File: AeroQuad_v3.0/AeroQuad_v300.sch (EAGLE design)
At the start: 68 parts, among them U1 MPU-6050-1

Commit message: Eagle files including CAM file for latest beta run of AeroQuad32 boards.
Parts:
- removed ACCEL: BMA180, SparkFun:M08LOCK
- removed GYRO: ITG3200, SparkFun:M07LOCK
- removed LED: ULN2003A, CaranchoEngineering:ULN2003A
- removed LED_GND, LED_PWR: (no value), SparkFun:M07LOCK
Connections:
- removed net N$10: LED.P$10, LED_GND.7
- removed net N$11: LED.P$11, LED_GND.6
- removed net N$12: LED.P$12, LED_GND.5
- removed net N$13: LED.P$13, LED_GND.4
- removed net N$14: LED.P$14, LED_GND.3
- removed net N$17: LED.P$15, LED_GND.2
- removed net P$16: LED.P$16, LED_GND.1
- net 3.3V: no longer ACCEL.1, ACCEL.4, ACCEL.8, GYRO.6, GYRO.7
- net GND: no longer ACCEL.2, ACCEL.6, GYRO.3, GYRO.5, LED.P$8
- net LED1: no longer LED.P$7
- net LED2: no longer LED.P$6
- net LED3: no longer LED.P$5
- net LED4: no longer LED.P$4
- net LED5: no longer LED.P$3
- net LED6: no longer LED.P$2
- net LED7: no longer LED.P$1
- net SCL-L: no longer ACCEL.5, GYRO.1
- net SDA-L: no longer ACCEL.7, GYRO.2
- net VIN: no longer LED_PWR.1, LED_PWR.2, LED_PWR.3, LED_PWR.4, LED_PWR.5, LED_PWR.6, LED_PWR.7

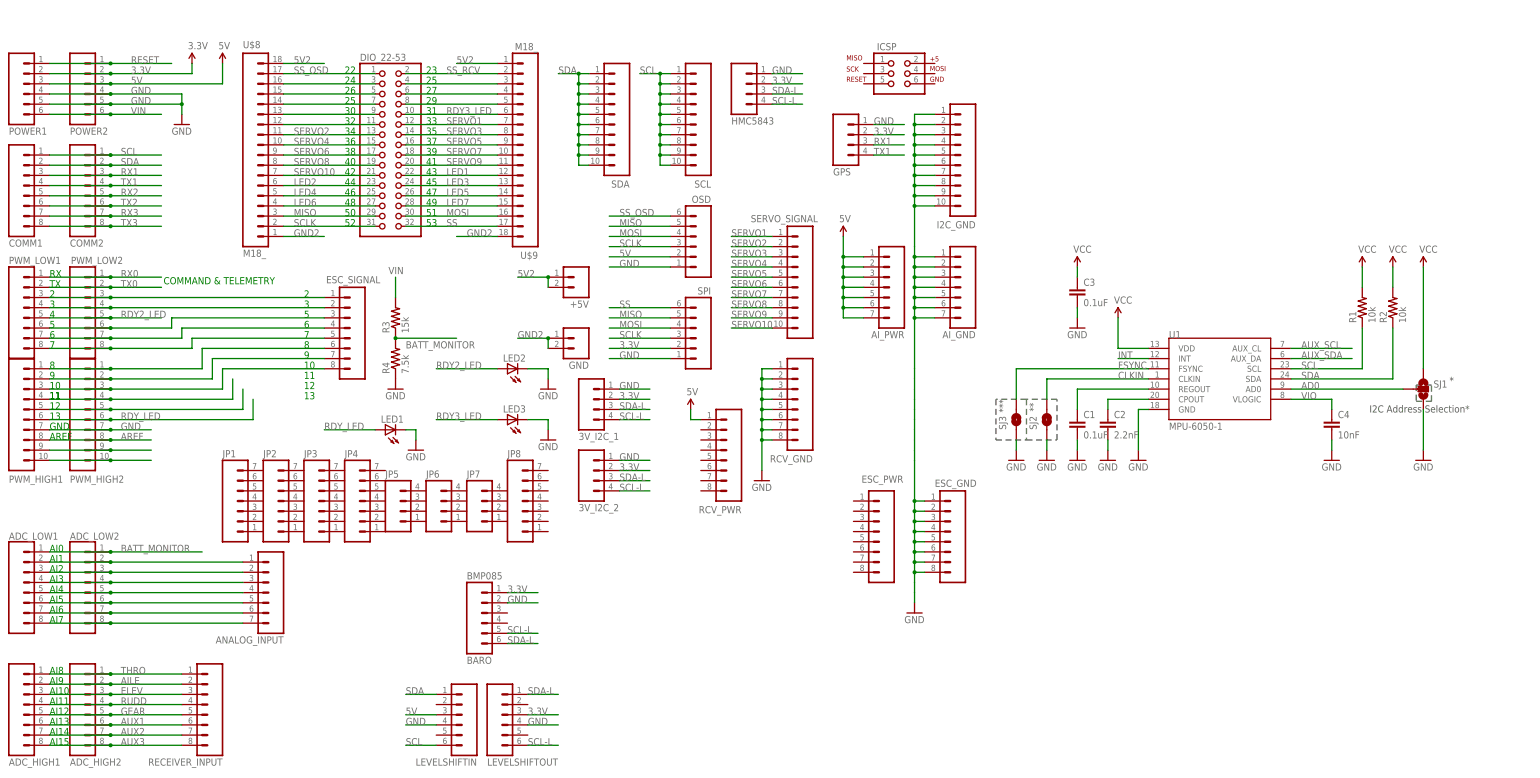
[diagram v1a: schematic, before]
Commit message: reviewed MPU6000 circuit and connections to Due
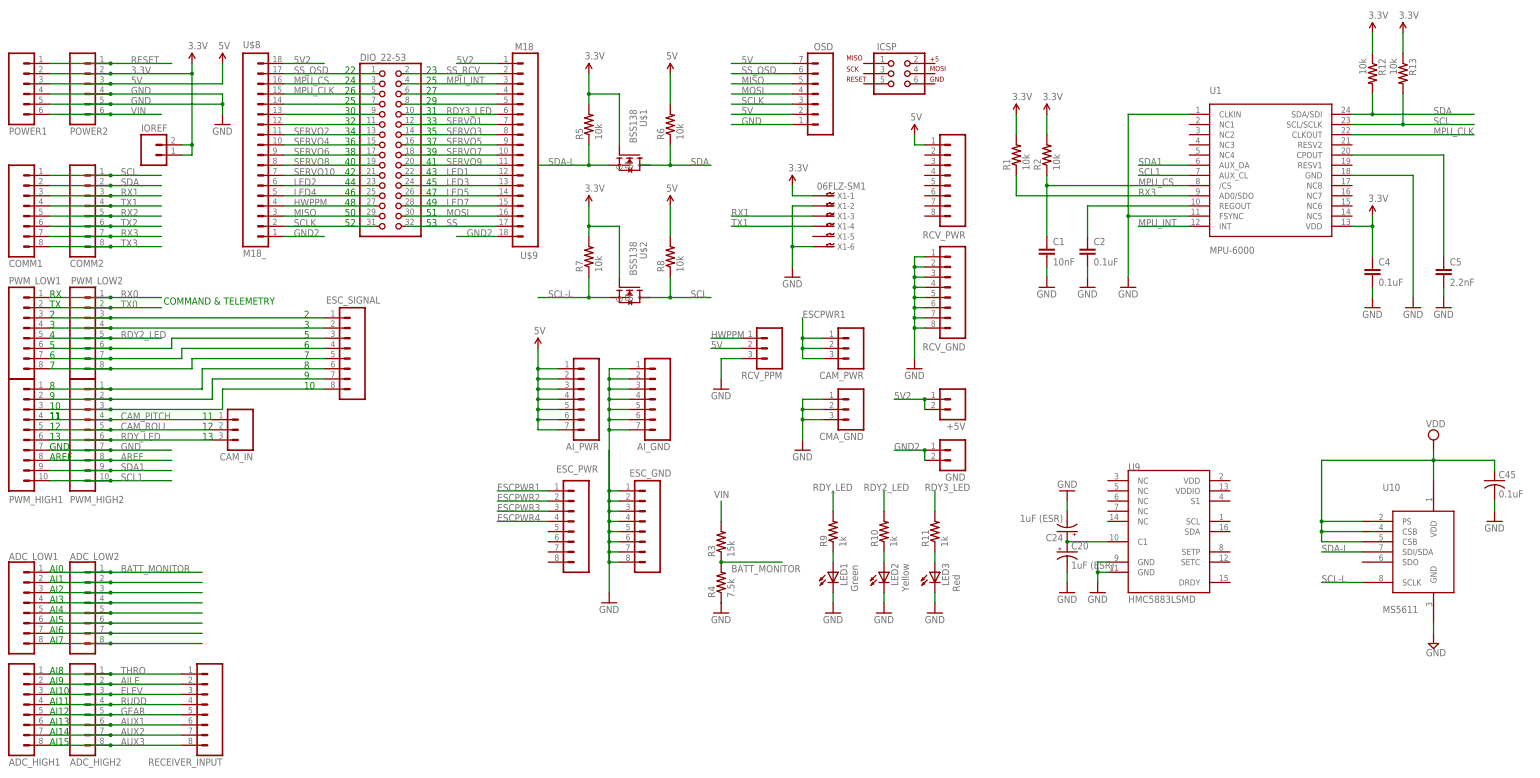
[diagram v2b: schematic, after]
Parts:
- removed 3V_I2C_1, 3V_I2C_2, GPS, HMC5843: (no value), SparkFun:M04LOCK
- removed ANALOG_INPUT, JP1, JP2, JP3, JP4, JP8: (no value), SparkFun:M07
- removed BARO: BMP085, SparkFun:M06LOCK
- removed C3: 0.1uF, SparkFun:CAP0402-CAP
- removed I2C_GND, SCL, SDA, SERVO_SIGNAL: M10LOCK, SparkFun:M10LOCK
- removed JP5, JP6, JP7: (no value), SparkFun:M04PTH
- removed LEVELSHIFTIN, LEVELSHIFTOUT, SPI: (no value), SparkFun:M06LOCK
- removed SJ1: (no value), SparkFun:SOLDERJUMPER_2WAYPASTE2&3
- removed SJ2, SJ3: SOLDERJUMPERTRACE, SparkFun:SOLDERJUMPERTRACE
- added C20, C24: 1uF (ESR), rcl:CPOL-USSMCZ
- added C45: 0.1uF, rcl:C-USC0402
- added C5: 2.2nF, SparkFun:CAP0402-CAP
- added CAM_IN, CAM_PWR, CMA_GND, RCV_PPM: (no value), SparkFun:M03LOCK
- added IOREF: (no value), SparkFun:M02LOCK
- added R10, R11, R9: 1k, SparkFun:RESISTOR0402-RES
- added R12, R13, R5, R6, R7, R8: 10k, SparkFun:RESISTOR0402-RES
- added U$1, U$2: BSS138, ava:BSS138
- added U10: MS5611, DSP-TI:MS5611
- added U9: HMC5883LSMD, SparkFun:HMC5883LSMD
- added X1: 06FLZ-SM1, con-jst:06FLZ-SM1
- C1: value 0.1uF -> 10nF
- C2: value 2.2nF -> 0.1uF
- C4: value 10nF -> 0.1uF
- LED1: value (none) -> Green; device SparkFun:LED5MM -> SparkFun:LED0603
- LED2: value (none) -> Yellow; device SparkFun:LED5MM -> SparkFun:LED0603
- LED3: value (none) -> Red; device SparkFun:LED5MM -> SparkFun:LED0603
- OSD: device SparkFun:M06LOCK -> SparkFun:M07LOCK
- R3, R4: device resistor:R-US_0204/5 -> SparkFun:RESISTOR0402-RES
- U1: value MPU-6050-1 -> MPU-6000; device Testing:MPU-6050-1 -> 3DRobotics_Master_Library:MPU-6000
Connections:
- removed net AD0: SJ1.2, U1.AD0
- removed net AUX_SCL: U1.AUX_CL
- removed net AUX_SDA: U1.AUX_DA
- removed net CLKIN: SJ2.2, U1.CLKIN
- removed net FSYNC: SJ3.2, U1.FSYNC
- removed net INT: U1.INT
- removed net LED6: DIO_22-53.27, U$8.4
- removed net N$15: DIO_22-53.3, U$8.16
- removed net N$20: DIO_22-53.5, U$8.15
- removed net N$22: DIO_22-53.4, U$9.3
- removed net N$28: PWM_HIGH1.4, PWM_HIGH2.4
- removed net N$29: PWM_HIGH1.5, PWM_HIGH2.5
- removed net N$30: PWM_HIGH1.9, PWM_HIGH2.9
- removed net N$31: PWM_HIGH1.10, PWM_HIGH2.10
- removed net N$32: C2.1, U1.CPOUT
- removed net VCC: C3.1, R1.2, R2.2, SJ1.1, U1.VDD
- removed net VIO: C4.1, U1.VLOGIC
- new net 3V3DIG: C45.1, U10.CSB, U10.CSB@2, U10.PS, U10.VDD
- new net CAM_PITCH: CAM_IN.1, PWM_HIGH1.4, PWM_HIGH2.4
- new net CAM_ROLL: CAM_IN.2, PWM_HIGH1.5, PWM_HIGH2.5
- new net ESCPWR1: CAM_PWR.1, CAM_PWR.2, CAM_PWR.3, ESC_PWR.1
- new net ESCPWR2: ESC_PWR.2
- new net ESCPWR3: ESC_PWR.3
- new net ESCPWR4: ESC_PWR.4
- new net HWPPM: DIO_22-53.27, RCV_PPM.1, U$8.4
- new net MPU_CLK: DIO_22-53.5, U$8.15, U1.CLKOUT
- new net MPU_CS: C1.1, DIO_22-53.3, R2.1, U$8.16, U1./CS
- new net MPU_INT: DIO_22-53.4, U$9.3, U1.INT
- new net N$10: LED1.A, R9.1
- new net N$11: LED2.A, R10.1
- new net N$12: LED3.A, R11.1
- new net N$40: C5.1, U1.CPOUT
- new net N$67: C20.+, C24.+, U9.C1
- new net SCL1: PWM_HIGH1.10, PWM_HIGH2.10, U1.AUX_CL
- new net SDA1: PWM_HIGH1.9, PWM_HIGH2.9, U1.AUX_DA
- net 3.3V: now also C4.1, IOREF.1, IOREF.2, R1.2, R12.1, R13.1, R2.2, R5.2, R7.2, U$1.G, U$2.G, U1.VDD, X1-1.1; no longer 3V_I2C_1.2, 3V_I2C_2.2, BARO.1, GPS.2, HMC5843.2, LEVELSHIFTOUT.3, SPI.2
- net 5V: now also OSD.7, R6.2, R8.2, RCV_PPM.2; no longer LEVELSHIFTIN.3
- net GND: now also C20.-, C24.-, C45.2, C5.2, CMA_GND.1, CMA_GND.2, CMA_GND.3, RCV_PPM.3, U1.CLKIN, U1.FSYNC, U10.GND, U9.GND@1, U9.GND@2, X1-2.1, X1-6.1; no longer 3V_I2C_1.1, 3V_I2C_2.1, BARO.2, C3.2, GPS.1, HMC5843.1, I2C_GND.1, I2C_GND.10, I2C_GND.2, I2C_GND.3, I2C_GND.4, I2C_GND.5, I2C_GND.6, I2C_GND.7, I2C_GND.8, I2C_GND.9, LEVELSHIFTIN.4, LEVELSHIFTOUT.4, SJ1.3, SJ2.1, SJ3.1, SPI.1
- net MISO: no longer SPI.5
- net MOSI: no longer SPI.4
- net N$18: no longer ANALOG_INPUT.6
- net N$19: no longer ANALOG_INPUT.7
- net N$33: now also C2.1; no longer C1.1
- net N$4: no longer ANALOG_INPUT.1
- net N$6: no longer ANALOG_INPUT.2
- net N$7: no longer ANALOG_INPUT.3
- net N$8: no longer ANALOG_INPUT.4
- net N$9: no longer ANALOG_INPUT.5
- net RDY2_LED: now also R10.2; no longer LED2.A
- net RDY3_LED: now also R11.2; no longer LED3.A
- net RDY_LED: now also CAM_IN.3, R9.2; no longer LED1.A
- net RX1: now also X1-3.1; no longer GPS.3
- net RX3: now also R1.1, U1.AD0/SDO
- net SCL: now also R13.2, R8.1, U$2.D, U1.SCL/SCLK; no longer LEVELSHIFTIN.6, R1.1, SCL.1, SCL.10, SCL.2, SCL.3, SCL.4, SCL.5, SCL.6, SCL.7, SCL.8, SCL.9, U1.SCL
- net SCL-L: now also R7.1, U$2.S, U10.SCLK; no longer 3V_I2C_1.4, 3V_I2C_2.4, BARO.5, HMC5843.4, LEVELSHIFTOUT.6
- net SCLK: no longer SPI.3
- net SDA: now also R12.2, R6.1, U$1.D, U1.SDA/SDI; no longer LEVELSHIFTIN.1, R2.1, SDA.1, SDA.10, SDA.2, SDA.3, SDA.4, SDA.5, SDA.6, SDA.7, SDA.8, SDA.9, U1.SDA
- net SDA-L: now also R5.1, U$1.S, U10.SDI/SDA; no longer 3V_I2C_1.3, 3V_I2C_2.3, BARO.6, HMC5843.3, LEVELSHIFTOUT.1
- net SERVO1: no longer SERVO_SIGNAL.1
- net SERVO10: no longer SERVO_SIGNAL.10
- net SERVO2: no longer SERVO_SIGNAL.2
- net SERVO3: no longer SERVO_SIGNAL.3
- net SERVO4: no longer SERVO_SIGNAL.4
- net SERVO5: no longer SERVO_SIGNAL.5
- net SERVO6: no longer SERVO_SIGNAL.6
- net SERVO7: no longer SERVO_SIGNAL.7
- net SERVO8: no longer SERVO_SIGNAL.8
- net SERVO9: no longer SERVO_SIGNAL.9
- net SS: no longer SPI.6
- net TX1: now also X1-4.1; no longer GPS.4
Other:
- note removed: "*"
- note removed: "**"
- note removed: "***"
- note removed: "I2C Address Selection*"
- moved on the sheet: +5V, ADC_LOW1, ADC_LOW2, AI_GND, AI_PWR, C1, C2, C4, COMM1, COMM2, ESC_GND, ESC_PWR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

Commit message: updated v2.1.3 shield with fixed 3.3V for GPS and added 5V reset line for OSD
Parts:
- removed C20, C24: 1uF (ESR), rcl:CPOL-USSMCZ
- removed C45: 0.1uF, rcl:C-USC0402
- removed R13: 10k, SparkFun:RESISTOR0402-RES
- added C3, C7: 0.1uF, SparkFun:CAP0402-CAP
- added C6: 0.22uF, SparkFun:CAP0402-CAP
- added C8: 100nF, SparkFun:CAP0402-CAP
- added EXT_MAG, GPS: (no value), SparkFun:M04LOCK
- added GPSBAT: (no value), SparkFun:M02PTH
- added LED4: Green, SparkFun:LED0603
- C4: value 0.1uF -> 2.2nF
- C5: value 2.2nF -> 4.7uF
- R12: value 10k -> 1k
- renumbered CMA_GND to CAM_GND
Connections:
- net N$18 renamed AI6
- net N$19 renamed AI7
- net N$4 renamed AI1
- net N$6 renamed AI2
- net N$7 renamed AI3
- net N$8 renamed AI4
- net N$9 renamed AI5
- removed net 3V3DIG: C45.1, U10.CSB, U10.CSB@2, U10.PS, U10.VDD
- removed net N$67: C20.+, C24.+, U9.C1
- new net GLED: R12.2, X1-6.1
- new net N$13: C5.1, U9.C1
- new net N$14: EXT_MAG.4, U1.AUX_CL
- new net N$15: EXT_MAG.3, U1.AUX_DA
- new net N$17: IOREF.1, IOREF.2
- new net N$20: C6.1, U9.SETP
- new net N$22: C6.2, U9.SETC
- new net N$4: LED4.A, R12.1
- new net N$8: GPSBAT.2, X1-5.1
- net 3.3V: now also C3.1, C7.1, C8.1, EXT_MAG.2, GPS.1, U10.CSB, U10.CSB@2, U10.PS, U10.VDD, U9.S1, U9.VDD, U9.VDDIO, X1-4.1; no longer C4.1, IOREF.1, IOREF.2, R12.1, R13.1, X1-1.1
- net GND: now also C3.2, C7.2, C8.2, EXT_MAG.1, GPS.2, GPSBAT.1, LED4.C, X1-3.1; no longer C20.-, C24.-, C45.2, X1-2.1, X1-6.1
- net N$40: now also C4.1; no longer C5.1
- net RX1: now also GPS.3, X1-2.1; no longer X1-3.1
- net SCL: no longer R13.2, U1.SCL/SCLK
- net SCL-L: now also U1.SCL/SCLK, U9.SCL
- net SCL1: no longer U1.AUX_CL
- net SDA: no longer R12.2, U1.SDA/SDI
- net SDA-L: now also U1.SDA/SDI, U9.SDA
- net SDA1: no longer U1.AUX_DA
- net TX1: now also GPS.4, X1-1.1; no longer X1-4.1
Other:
- note added: "GPS"
- note added: "LED"
- note added: "VBAT"
- note added: "VIN"
- moved on the sheet: AI_GND, AI_PWR, C1, C2, C4, C5, ESC_GND, ESC_PWR, R1, R12, R2, R3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

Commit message: Begin work on Due compatible AQ shield
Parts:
- removed R5, R6, R7, R8: 10k, SparkFun:RESISTOR0402-RES
- removed U$1, U$2: BSS138, ava:BSS138
- added IC3: 74245MTC, adafruit:74245MTC
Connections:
- removed net CAM_PITCH: CAM_IN.1, PWM_HIGH1.4, PWM_HIGH2.4
- removed net CAM_ROLL: CAM_IN.2, PWM_HIGH1.5, PWM_HIGH2.5
- removed net HWPPM: DIO_22-53.27, RCV_PPM.1, U$8.4
- removed net N$16: ESC_SIGNAL.3, PWM_LOW1.6, PWM_LOW2.6
- removed net N$21: ESC_SIGNAL.1, PWM_LOW1.3, PWM_LOW2.3
- removed net N$23: ESC_SIGNAL.4, PWM_LOW1.7, PWM_LOW2.7
- removed net N$24: ESC_SIGNAL.5, PWM_LOW1.8, PWM_LOW2.8
- removed net N$25: ESC_SIGNAL.6, PWM_HIGH1.1, PWM_HIGH2.1
- removed net N$26: ESC_SIGNAL.7, PWM_HIGH1.2, PWM_HIGH2.2
- removed net N$27: ESC_SIGNAL.8, PWM_HIGH1.3, PWM_HIGH2.3
- removed net SCL: COMM1.1, COMM2.1, R8.1, U$2.D
- removed net SDA: COMM1.2, COMM2.2, R6.1, U$1.D
- removed net SERVO2: DIO_22-53.13, U$8.11
- removed net SERVO4: DIO_22-53.15, U$8.10
- removed net SERVO6: DIO_22-53.17, U$8.9
- removed net SERVO8: DIO_22-53.19, U$8.8
- new net PWM10: IC3A.A5, PWM_HIGH1.3, PWM_HIGH2.3
- new net PWM11: IC3A.A6, PWM_HIGH1.4, PWM_HIGH2.4
- new net PWM12: IC3A.A7, PWM_HIGH1.5, PWM_HIGH2.5
- new net PWM13: IC3A.A8, PWM_HIGH1.6, PWM_HIGH2.6
- new net PWM2: IC3A.A1, PWM_LOW1.3, PWM_LOW2.3
- new net PWM3: IC3A.A2, PWM_LOW1.4, PWM_LOW2.4
- new net PWM34: DIO_22-53.13, ESC_SIGNAL.4, U$8.11
- new net PWM36: DIO_22-53.15, ESC_SIGNAL.3, U$8.10
- new net PWM38: DIO_22-53.17, ESC_SIGNAL.2, U$8.9
- new net PWM4: IC3A.A3, PWM_LOW1.5, PWM_LOW2.5
- new net PWM40: DIO_22-53.19, ESC_SIGNAL.1, U$8.8
- new net PWM5: IC3A.A4, PWM_LOW1.6, PWM_LOW2.6
- new net PWM6: ESC_SIGNAL.5, PWM_LOW1.7, PWM_LOW2.7
- new net PWM7: ESC_SIGNAL.6, PWM_LOW1.8, PWM_LOW2.8
- new net PWM8: ESC_SIGNAL.7, PWM_HIGH1.1, PWM_HIGH2.1
- new net PWM9: ESC_SIGNAL.8, PWM_HIGH1.2, PWM_HIGH2.2
- net 3.3V: now also IC3P.VCC; no longer R5.2, R7.2, U$1.G, U$2.G
- net 5V: no longer R6.2, R8.2
- net AILE: now also IC3A.B7; no longer ADC_HIGH1.2, ADC_HIGH2.2
- net AUX1: now also IC3A.B3; no longer ADC_HIGH1.6, ADC_HIGH2.6
- net AUX2: now also IC3A.B2; no longer ADC_HIGH1.7, ADC_HIGH2.7
- net AUX3: now also IC3A.B1; no longer ADC_HIGH1.8, ADC_HIGH2.8
- net ELEV: now also IC3A.B6; no longer ADC_HIGH1.3, ADC_HIGH2.3
- net GEAR: now also IC3A.B4; no longer ADC_HIGH1.5, ADC_HIGH2.5
- net GND: now also IC3A.DIR, IC3A.G, IC3P.GND
- net N$5: now also DIO_22-53.27, U$8.4; no longer ESC_SIGNAL.2, PWM_LOW1.4, PWM_LOW2.4
- net RDY2_LED: no longer PWM_LOW1.5, PWM_LOW2.5
- net RDY_LED: no longer CAM_IN.3, PWM_HIGH1.6, PWM_HIGH2.6
- net RUDD: now also IC3A.B5; no longer ADC_HIGH1.4, ADC_HIGH2.4
- net SCL-L: now also COMM1.1, COMM2.1; no longer R7.1, U$2.S
- net SDA-L: now also COMM1.2, COMM2.2; no longer R5.1, U$1.S
- net THRO: now also IC3A.B8, RCV_PPM.1; no longer ADC_HIGH1.1, ADC_HIGH2.1
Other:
- note added: "* SN74LVC245A - Octal Transceiver(296-1231-1-ND) Receiver Input, PWM: 2,3,4,5,10,11,12,13"
- note added: "All AQ functions on each pin need to be reviewed All Arduino pin functions should be the same (still needs review, especially voltage)"
- note added: "Motor ESC's, PWM: 6,7,8,9,34,36,38,40"
- moved on the sheet: ESC_SIGNAL, RCV_PPM, RECEIVER_INPUT

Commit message: added camera servo pins, starting overall review of other Due pins
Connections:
- net SCL1 renamed SCL1-L
- net SDA1 renamed SDA1-L
- removed net LED2: DIO_22-53.23, U$8.6
- removed net SERVO10: DIO_22-53.21, U$8.7
- removed net SS: DIO_22-53.32, U$9.17
- new net CAM1: CAM_IN.1, DIO_22-53.21, U$8.7
- new net CAM2: CAM_IN.2, DIO_22-53.23, U$8.6
- new net CAM3: CAM_IN.3, DIO_22-53.32, U$9.17
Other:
- note added: "Cam Servo: 42,44,53"
- note removed: "COMMAND & TELEMETRY"
- moved on the sheet: CAM_IN, GPS, GPSBAT, IC3, IC3P, RCV_PPM, RECEIVER_INPUT, X1-1, X1-2, X1-3, X1-4, X1-5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
